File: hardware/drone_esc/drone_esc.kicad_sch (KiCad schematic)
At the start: 0 parts

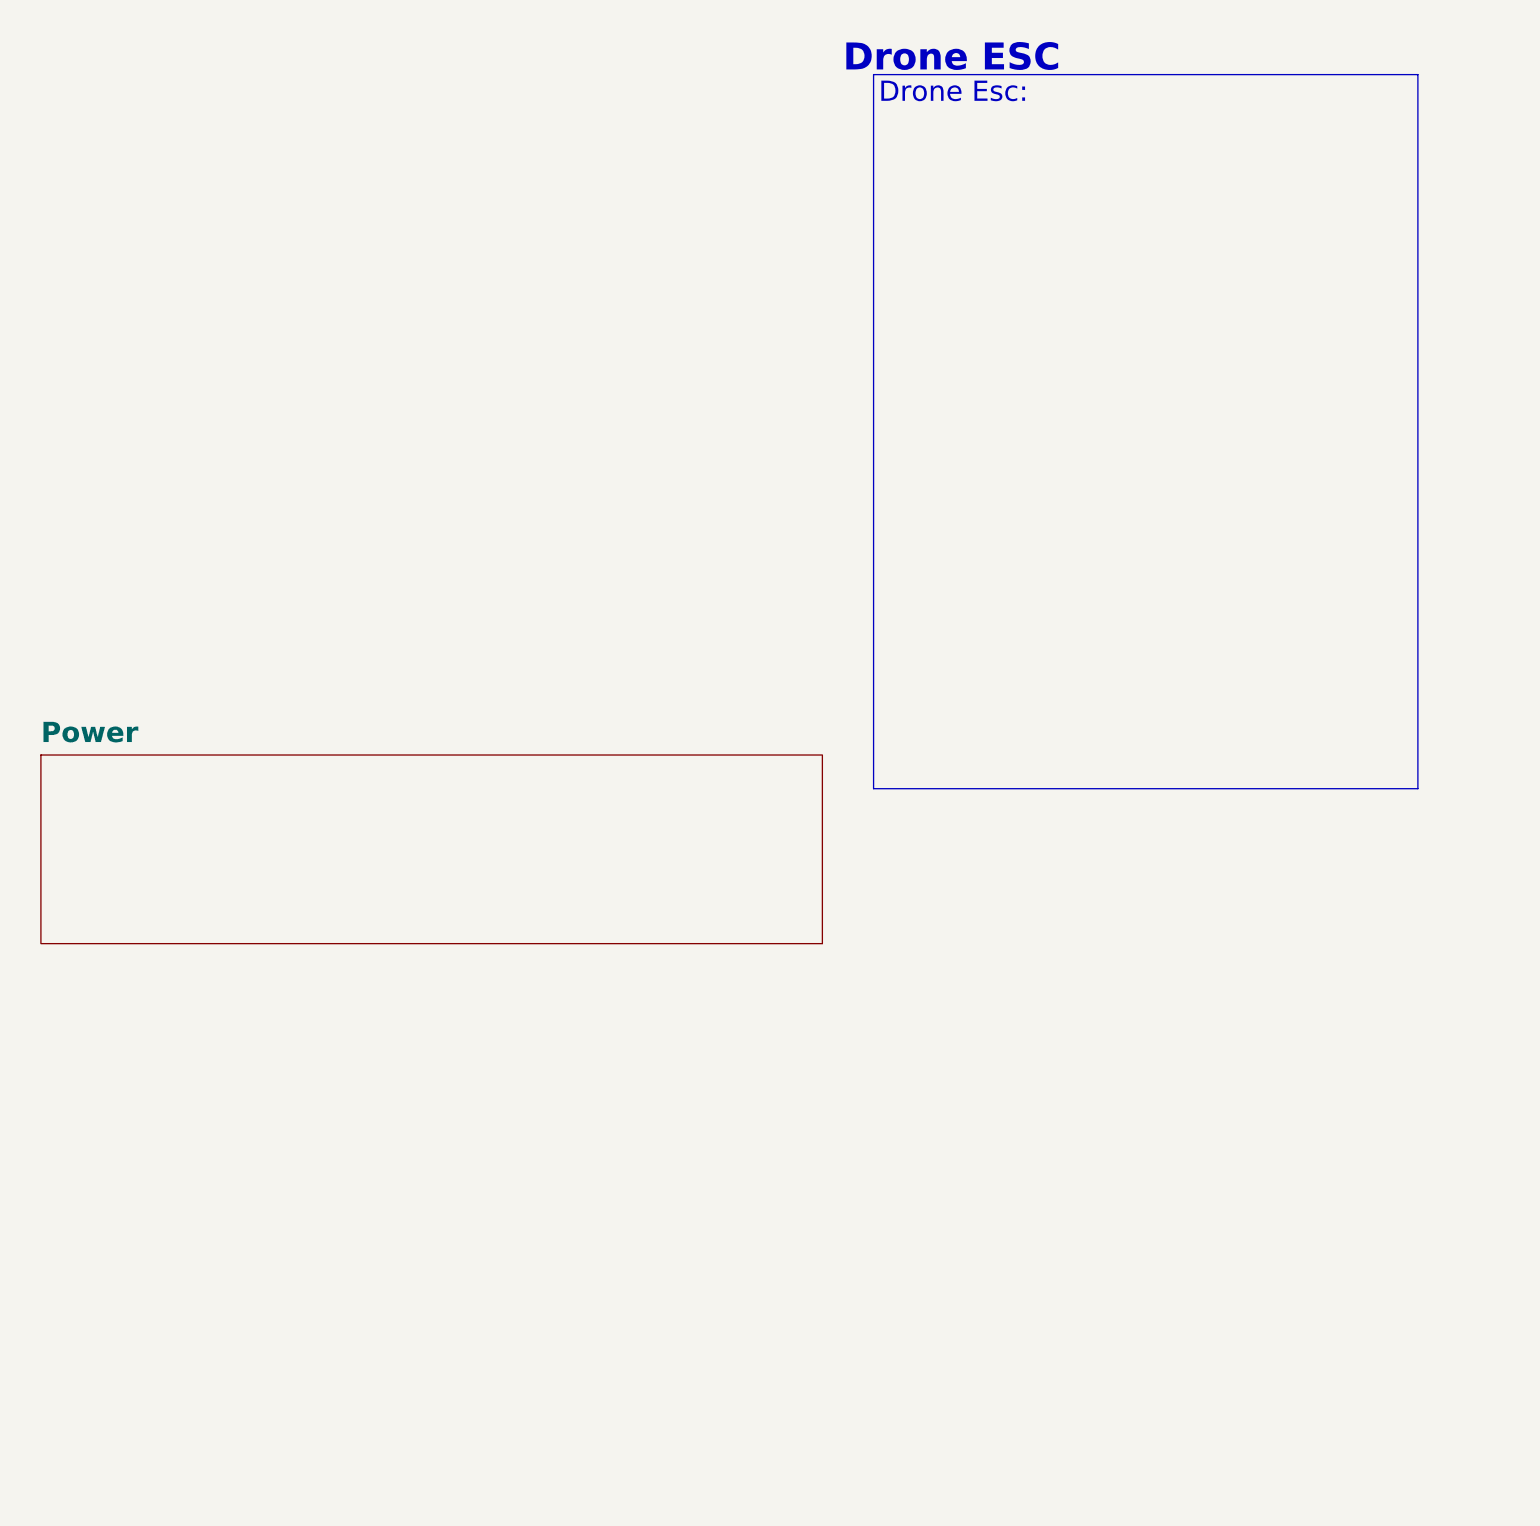
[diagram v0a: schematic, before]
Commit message: created schematic hierarchy
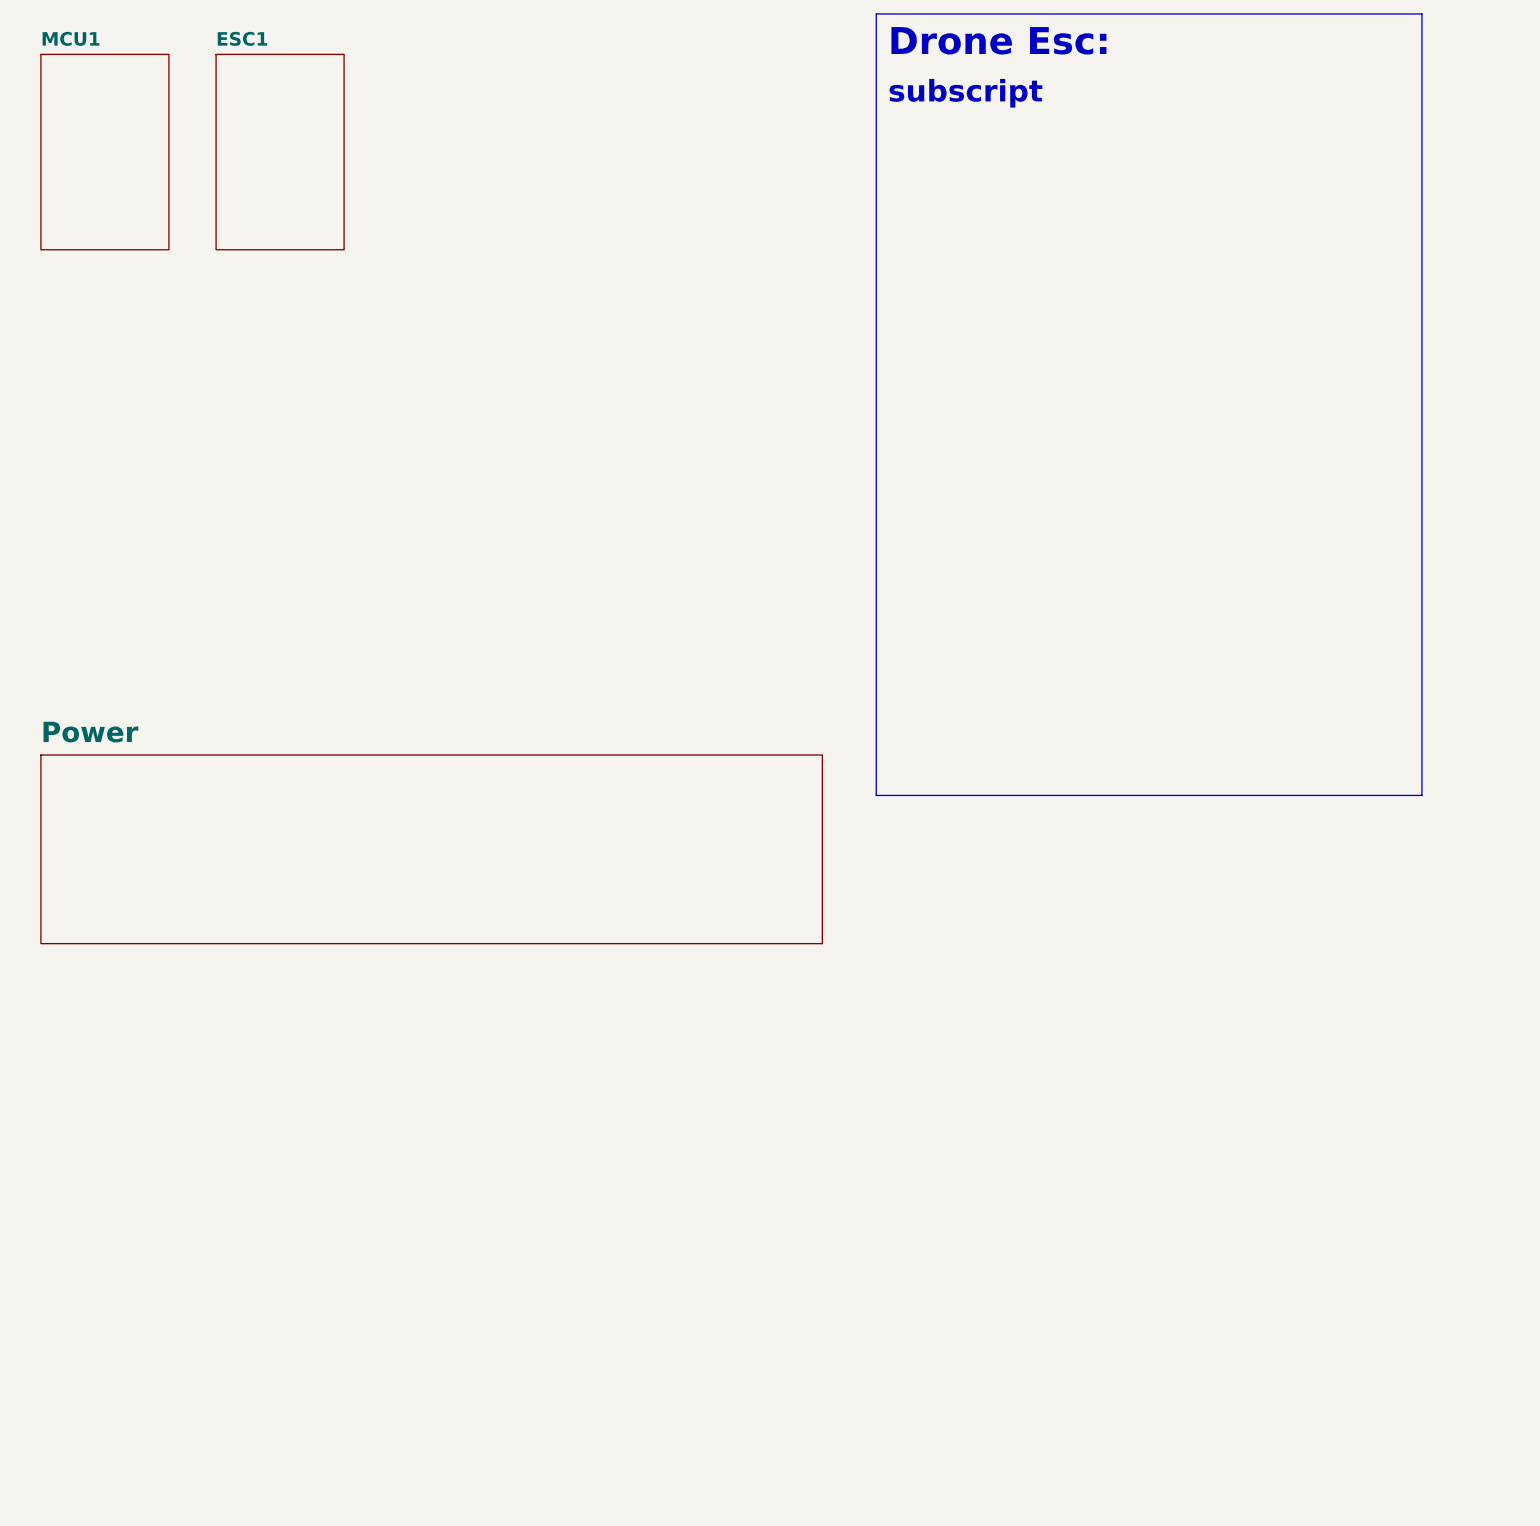
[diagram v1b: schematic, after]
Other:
- added sheet ESC1 (schematics/esc_1.kicad_sch)
- added sheet MCU1 (schematics/mcu_1.kicad_sch)
- sheet Power: file power.kicad_sch -> schematics/power.kicad_sch
- note removed: "Drone ESC"
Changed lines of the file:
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@@
 	(generator_version "9.0")
 	(paper "A4")
-	(text "Drone ESC\n\n"
-		(exclude_from_sim no)
-		(at 192.024 27.686 0)
-		(effects
-			(font
-				(face "Agency FB")
-				(size 5.08 5.08)
-				(bold yes)
-			)
+	(rectangle
+		(start 177.8 15.24)
+		(end 280.67 162.56)
+		(stroke
+			(width 0)
+			(type default)
+		)
+		(fill
+			(type none)
 		)
 	)
-	(text_box "Drone Esc:"
+	(text_box "Drone Esc:\n_{subscript}"
 		(exclude_from_sim no)
-		(at 177.292 26.67 0)
-		(size 102.616 134.62)
+		(at 179.07 16.51 0)
+		(size 100.33 144.78)
 		(margins 0.9525 0.9525 0.9525 0.9525)
 		(stroke
-			(width 0)
+			(width -0.0001)
 			(type solid)
 		)
@@
 		(effects
 			(font
-				(size 3.81 3.81)
+				(face "Agency FB")
+				(size 5.08 5.08)
+				(bold yes)
 			)
 			(justify left top)
+		)
+	)
+	(sheet
+		(at 53.34 22.86)
+		(size 24.13 36.83)
+		(exclude_from_sim no)
+		(in_bom yes)
+		(on_board yes)
+		(dnp no)
+		(fields_autoplaced yes)
+		(stroke
+			(width 0.1524)
+			(type solid)
+		)
+		(fill
+			(color 0 0 0 0.0000)
+		)
+		(property "Sheetname" "ESC1"
+			(at 53.34 21.5134 0)
+			(effects
+				(font
+					(face "Agency FB")
+					(size 2.54 2.54)
+					(thickness 0.508)
+					(bold yes)
+				)
+				(justify left bottom)
+			)
+		)
+		(property "Sheetfile" "schematics/esc_1.kicad_sch"
+			(at 53.34 60.2746 0)
+			(effects
+				(font
+					(size 1.27 1.27)
+				)
+				(justify left top)
+				(hide yes)
+			)
+		)
+		(instances
+			(project "drone_esc"
+				(path "/b5a13fd4-6868-4fff-a56c-eae40f1d53c7"
+					(page "4")
+				)
+			)
 		)
 	)
@@
 			(effects
 				(font
+					(face "Agency FB")
 					(size 3.81 3.81)
 					(thickness 0.762)
@@
 			)
 		)
-		(property "Sheetfile" "power.kicad_sch"
+		(property "Sheetfile" "schematics/power.kicad_sch"
 			(at 20.32 191.0846 0)
 			(effects
@@
 				)
 			)
+		)
+	)
+	(sheet
+		(at 20.32 22.86)
+		(size 24.13 36.83)
+		(exclude_from_sim no)
+		(in_bom yes)
+		(on_board yes)
+		(dnp no)
+		(fields_autoplaced yes)
+		(stroke
+			(width 0.1524)
+			(type solid)
+		)
+		(fill
+			(color 0 0 0 0.0000)
+		)
+		(property "Sheetname" "MCU1"
+			(at 20.32 21.5134 0)
+			(effects
+				(font
+					(face "Agency FB")
+					(size 2.54 2.54)
+					(thickness 0.508)
+					(bold yes)
+				)
+				(justify left bottom)
+			)
+		)
+		(property "Sheetfile" "schematics/mcu_1.kicad_sch"
+			(at 20.32 60.2746 0)
+			(effects
+				(font
+					(size 1.27 1.27)
+				)
+				(justify left top)
+				(hide yes)
+			)
+		)
+		(instances
+			(project "drone_esc"
+				(path "/b5a13fd4-6868-4fff-a56c-eae40f1d53c7"
+					(page "3")
+				)
+			)

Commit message: Added footprint and symbol libraries
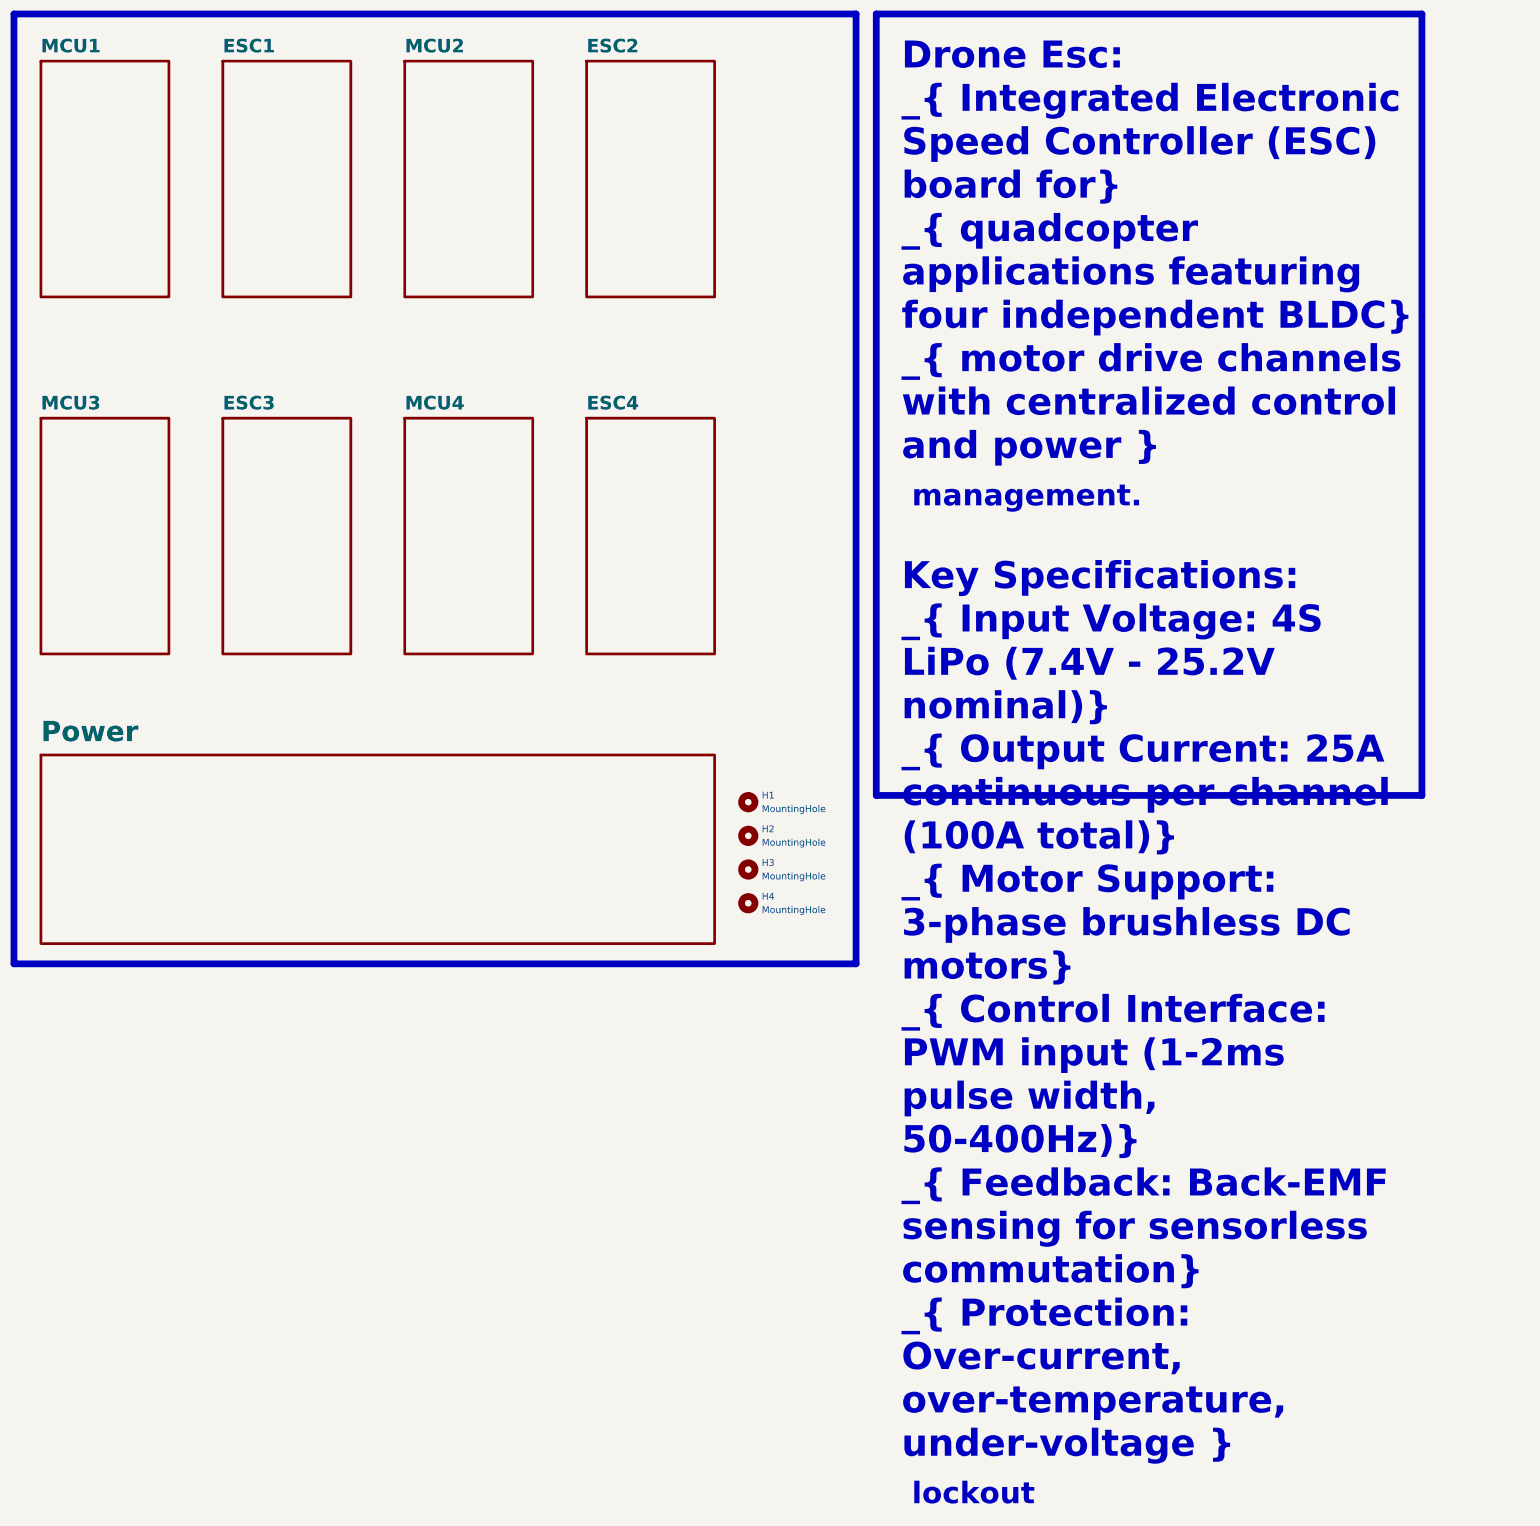
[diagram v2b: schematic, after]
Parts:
- added H1, H2, H3, H4: MountingHole, symbol Mechanical:MountingHole
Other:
- added sheet ESC2 (schematics/esc_2.kicad_sch)
- added sheet ESC3 (schematics/esc_3.kicad_sch)
- added sheet ESC4 (schematics/esc_4.kicad_sch)
- added sheet MCU2 (schematics/mcu_2.kicad_sch)
- added sheet MCU3 (schematics/mcu_3.kicad_sch)
- added sheet MCU4 (schematics/mcu_4.kicad_sch)
- company: (none) -> Daniel Development Space
- title: (none) -> Drone esc board overview

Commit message: created power schematics, assigned footprints and parts
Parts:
- H1, H2, H3, H4: footprint (none) -> MountingHole:MountingHole_3.2mm_M3
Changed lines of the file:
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@@
 			)
 		)
-		(property "Footprint" ""
+		(property "Footprint" "MountingHole:MountingHole_3.2mm_M3"
 			(at 153.67 170.18 0)
 			(effects
@@
 			)
 		)
-		(property "Footprint" ""
+		(property "Footprint" "MountingHole:MountingHole_3.2mm_M3"
 			(at 153.67 182.88 0)
 			(effects
@@
 			)
 		)
-		(property "Footprint" ""
+		(property "Footprint" "MountingHole:MountingHole_3.2mm_M3"
 			(at 153.67 176.53 0)
 			(effects
@@
 			)
 		)
-		(property "Footprint" ""
+		(property "Footprint" "MountingHole:MountingHole_3.2mm_M3"
 			(at 153.67 163.83 0)
 			(effects
